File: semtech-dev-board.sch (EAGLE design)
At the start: 62 parts, among them Q1 BSS123, Q2 32MHz, U1 SEMTECH_SX1236, U2 QUALCOMM-TDK_B3588, U3 MIC5219 3.3V, U4 QUALCOMM-TDK_B3710

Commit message: Tuesday D/R
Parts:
- removed C23: 1uF, rcl:C-USC0805
- removed C24, C26, C28: 100nF, rcl:C-USC0805
- removed C27: 10uF, rcl:C-USC0805
- removed CF1: (no value), psas_c3_team05:CON_USB-MICRO-B-RECEPTACLE-PTH-HIROSE-ZX62D-B-5P8
- removed Q2: 32MHz, low-gain-radio:CRYSTAL2.5X2.0MM
- removed S2: SWITCH-MOMENTARY-2SMD-2, psas_c3_team05:SWITCH-MOMENTARY-2SMD-2
- removed TP7: TEST-POINT, low-gain-radio:TEST-POINT
- removed U$1, U$2, U$3, U$4: SMAJ716-ND, psas_c3_team05:SMAJ716-ND
- added C1: 10uF, rcl:C-USC0805
- added C3: 1uF, rcl:C-USC0805
- added P1, P2, P3, P4: SMAJ716-ND, psas_c3_team05:SMAJ716-ND
- added P5: (no value), psas_c3_team05:CON_USB-MICRO-B-RECEPTACLE-PTH-HIROSE-ZX62D-B-5P8
- added S1: SWITCH-MOMENTARY-2SMD-2, psas_c3_team05:SWITCH-MOMENTARY-2SMD-2
- added TP3: TEST-POINT, low-gain-radio:TEST-POINT
- added Y1: 32MHz, low-gain-radio:CRYSTAL2.5X2.0MM
- C11: value 22pF -> 100nF
- C12: value 4.7pF -> 100nF
- C13: value 8.2pF -> 100nF
- C14: value 2.7pF -> 8.2pF
- C15: value ?? -> 10nF
- C16: value 15pF -> 6.8pF
- C17: value ?? -> 5.6pF
- C18: value 6.8pF -> 100nF
- C19: value ?? -> 100nF
- C20: value 8.2pF -> 4.7pF
- C21: value 470pF -> 15pF
- C22: value 5.6pF -> 15pF
- C4: value 100nF -> 470pF
- C5: value 100nF -> 2.7pF
- C6: value 6pF -> 22pF
- C7: value 6pF -> 15pF
- C8: value 10nF -> 8.2pF
- JP1: device pinhead:PINHD-1X7 -> pinhead:PINHD-1X2
- JP2: device pinhead:PINHD-1X4 -> pinhead:PINHD-1X2
- JP3, JP5: device pinhead:PINHD-1X2 -> pinhead:PINHD-1X4
- JP4: device pinhead:PINHD-1X4 -> pinhead:PINHD-1X8
- L1: value 33nH -> 12nH; device rcl:L-USL3230M -> rcl:L-USL3225M
- L2: value 33nH -> 10nH; device rcl:L-USL3230M -> rcl:L-USL3225M
- L3: value 10nH -> 33nH; device rcl:L-USL3230M -> rcl:L-USL3225M
- L4: value 3.9nH -> 10nH; device rcl:L-USL3230M -> rcl:L-USL3225P
- L5: value 12nH -> 33nH; device rcl:L-USL1812 -> rcl:L-USL3225P
- L6: device rcl:L-USL3230M -> rcl:L-USL3225M
- L7: value 10nH -> 6.8nH; device rcl:L-USL3230M -> rcl:L-USL3225M
- L8: value 6.8nH -> 3.9nH; device rcl:L-USL3230M -> rcl:L-USL3225M
- R1: value 1k -> 0
- R5: value 0 -> 1k
- U1: value SEMTECH_SX1236 -> MIC5219 3.3V; device low-gain-radio:SEMTECH_SX1236 -> SparkFun-IC-Power:V_REG_MIC52193.3V
- U2: value QUALCOMM-TDK_B3588 -> QUALCOMM-TDK_B3710; device low-gain-radio:QUALCOMM-TDK_B3588 -> low-gain-radio:QUALCOMM-TDK_B3710
- U3: value MIC5219 3.3V -> QUALCOMM-TDK_B3588; device SparkFun-IC-Power:V_REG_MIC52193.3V -> low-gain-radio:QUALCOMM-TDK_B3588
- U4: value QUALCOMM-TDK_B3710 -> SEMTECH_SX1236; device low-gain-radio:QUALCOMM-TDK_B3710 -> low-gain-radio:SEMTECH_SX1236
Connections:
- removed net DIO0: JP1.2, U1.DIO0
- removed net DIO1: JP1.3, U1.DIO1/DCLK
- removed net DIO2: JP1.4, U1.DIO2/DATA
- removed net DIO3: JP1.5, U1.DIO3
- removed net DIO4: JP1.6, U1.DIO4
- removed net DIO5: JP1.7, U1.DIO5
- new net N$2: JP4.8, U4.DIO5
- new net N$4: JP4.7, U4.DIO4
- new net N$6: JP4.6, U4.DIO3
- new net N$7: JP4.5, U4.DIO2/DATA
- new net N$8: JP4.4, U4.DIO1/DCLK
- new net N$9: JP4.3, U4.DIO0
- net +3V3: now also C3.1, R4.2, R5.2, TP6.1, U1.OUT; no longer C23.1, R1.2, R3.2, TP5.1, U3.OUT
- net BP: now also C4.1, U1.BP; no longer C21.1, U3.BP
- net GND: now also C1.2, C11.2, C13.2, C15.2, C17.2, C19.2, C3.2, JP1.2, JP2.2, P1.OUTERCONDUCTOR, P2.OUTERCONDUCTOR, P3.OUTERCONDUCTOR, P4.OUTERCONDUCTOR, P5.5, S1.1, U1.GND, U4.GND1, U4.GND2, U4.GND3, U4.GROUND; no longer C23.2, C24.2, C26.2, C27.2, C28.2, C5.2, C6.2, CF1.5, JP3.2, JP5.2, S2.1, U$1.OUTERCONDUCTOR, U$2.OUTERCONDUCTOR, U$3.OUTERCONDUCTOR, U$4.OUTERCONDUCTOR, U1.GND1, U1.GND2, U1.GND3, U1.GROUND, U4.GND
- net HFO_PA_HEAD: now also C15.1, JP3.4, L5.2; no longer C9.1, JP4.4, L2.2
- net LED+: now also R3.1; no longer R2.1
- net LFO_PA_HEAD: now also C9.1, JP3.1, L3.2; no longer C8.1, JP4.1, L1.2
- net N$1: now also R2.1, TP4.1, U1.EN; no longer R5.1, TP1.1, U3.EN
- net N$5: now also P1.CENTERCONDUCTOR, U2.OUT; no longer U$1.CENTERCONDUCTOR, U4.OUT
- net PA_BOOST: now also TP2.1, U4.PA_BOOST; no longer TP7.1, U1.PA_BOOST
- net RFI_HF: now also U3.IN, U4.RFI_HF; no longer U1.RFI_HF, U2.IN
- net RFI_HF_ANT: now also P4.CENTERCONDUCTOR, U3.OUT; no longer U$4.CENTERCONDUCTOR, U2.OUT
- net RFI_LF: now also U2.IN, U4.RFI_LF; no longer U1.RFI_LF, U4.IN
- net RFO_HF: now also L8.2, U4.RFO_HF; no longer L4.2, U1.RFO_HF
- net RFO_HF_1: now also C14.2; no longer C13.2, C15.1
- net RFO_HF_2: now also C16.1, L7.2; no longer C15.2, C18.1, C19.1, L8.2
- net RFO_HF_OUT: now also C17.1, L7.1, P3.CENTERCONDUCTOR; no longer C19.2, C22.1, L8.1, U$3.CENTERCONDUCTOR
- net RFO_HF_PA: now also C14.1, C20.1, L5.1, L8.1; no longer C12.1, C13.1, L2.1, L4.1
- net RFO_LF: now also L4.1, U4.RFO_LF; no longer L3.1, U1.RFO_LF
- net RFO_LF_1: now also C5.1, C6.2, L1.2; no longer C11.2, C14.1, L5.2
- net RFO_LF_2: now also C5.2, C7.1, L1.1, L2.2; no longer C14.2, C16.1, C17.1, L5.1, L7.2
- net RFO_LF_OUT: now also C8.1, L2.1, P2.CENTERCONDUCTOR; no longer C17.2, C20.1, L7.1, U$2.CENTERCONDUCTOR
- net RFO_LF_PA: now also C6.1, L3.1, L4.2; no longer C11.1, L1.1, L3.2
- net RXTX: now also JP2.1, JP4.2, U4.RXTX; no longer JP1.1, JP3.1, U1.RXTX
- net SPI_MISO: now also JP5.2, U4.MISO; no longer JP2.2, U1.MISO
- net SPI_MOSI: now also JP5.3, U4.MOSI; no longer JP2.3, U1.MOSI
- net SPI_NSS: now also JP5.4, U4.NSS; no longer JP2.4, U1.NSS
- net SPI_SCK: now also JP5.1, U4.SCK; no longer JP2.1, U1.SCK
- net SX1236_RST: now also JP4.1, R5.1, S1.2, TP1.1, U4.NRESET; no longer R1.1, S2.2, TP4.1, U1.NRESET
- net VBAT: now also C11.1, C12.1, C13.1, R3.2, R4.1, U4.VBAT_ANA, U4.VBAT_DIG, U4.VBAT_RF; no longer C2.1, C24.1, C26.1, R2.2, R3.1, U1.VBAT_ANA, U1.VBAT_DIG, U1.VBAT_RF
- net VREG_IN: now also C1.1, C2.1, R1.2, R2.2, TP5.1, U1.IN; no longer C27.1, C28.1, R4.2, R5.2, TP6.1, U3.IN
- net VR_ANA: now also C18.1, U4.VR_ANA; no longer C4.1, U1.VR_ANA
- net VR_DIG: now also C19.1, U4.VR_DIG; no longer C5.1, U1.VR_DIG
- net VR_PA: now also JP3.2, JP3.3, U4.VR_PA; no longer JP4.2, JP4.3, U1.VR_PA
- net V_IN: now also JP1.1, P5.1, R1.1, TP3.1; no longer CF1.1, JP5.1, R4.1, TP2.1
- net XTALA: now also C22.1, U4.XTA, Y1.2; no longer C7.1, Q2.2, U1.XTA
- net XTALB: now also C21.1, U4.XTB, Y1.1; no longer C6.1, Q2.1, U1.XTB
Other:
- moved on the sheet: C10, C11, C12, C13, C14, C15, C16, C17, C18, C19, C2, C20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

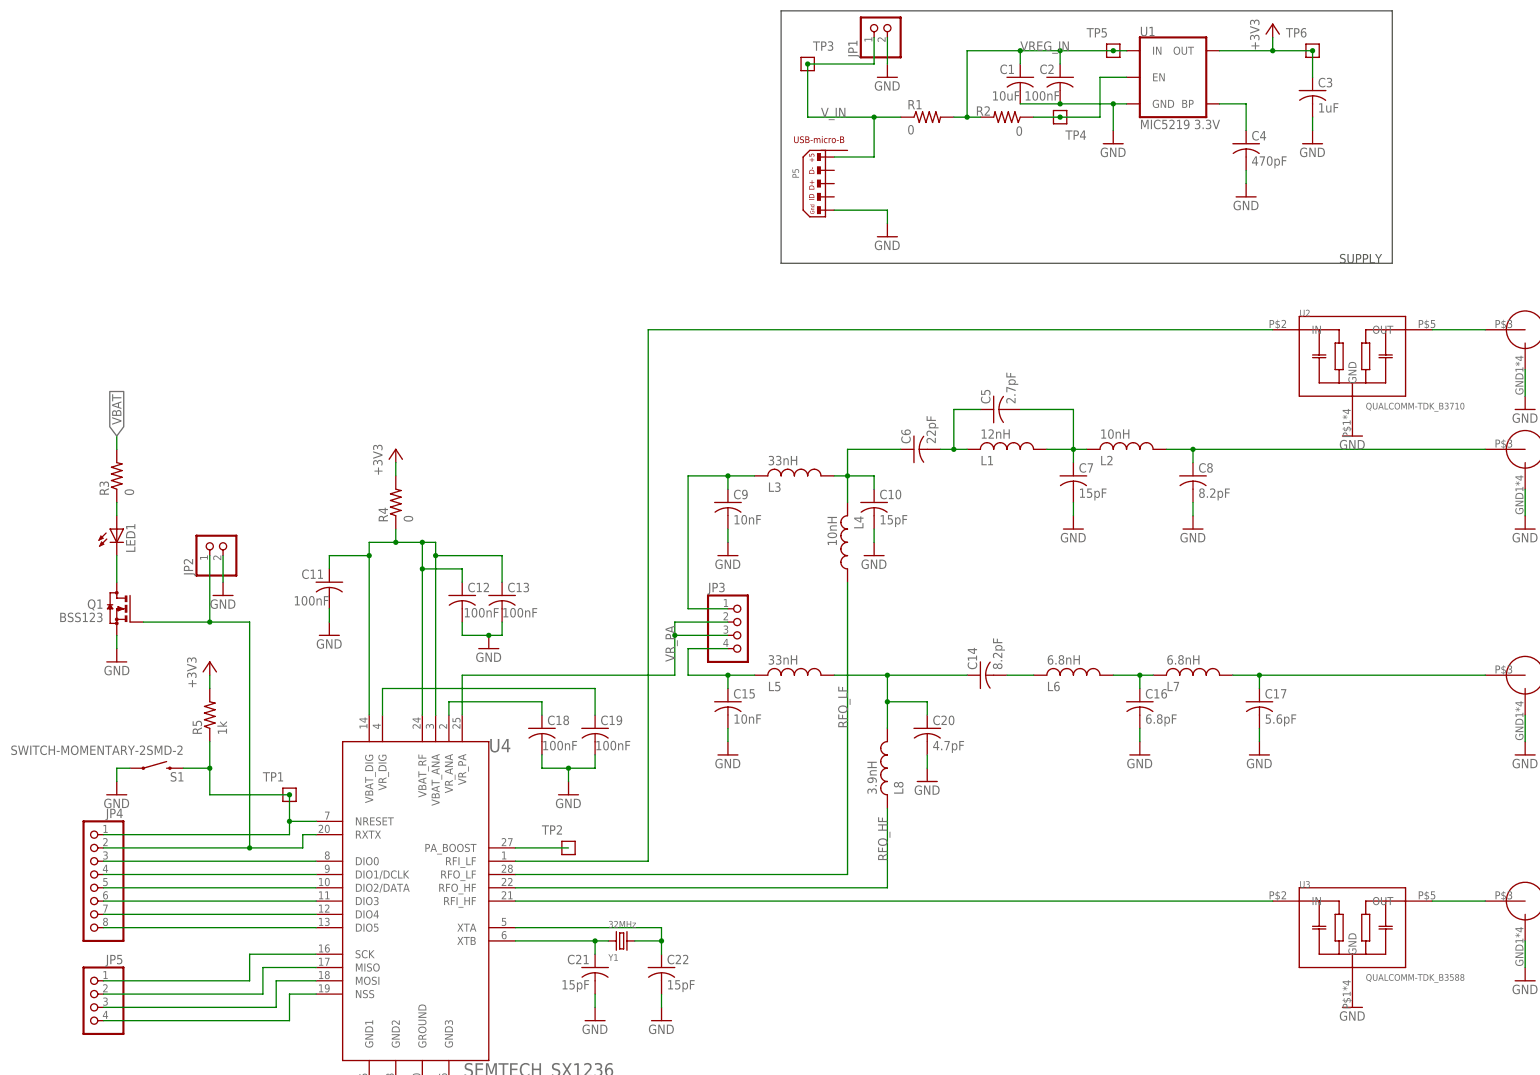
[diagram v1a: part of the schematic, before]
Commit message: reworked board based on feedback, needs mounting holes
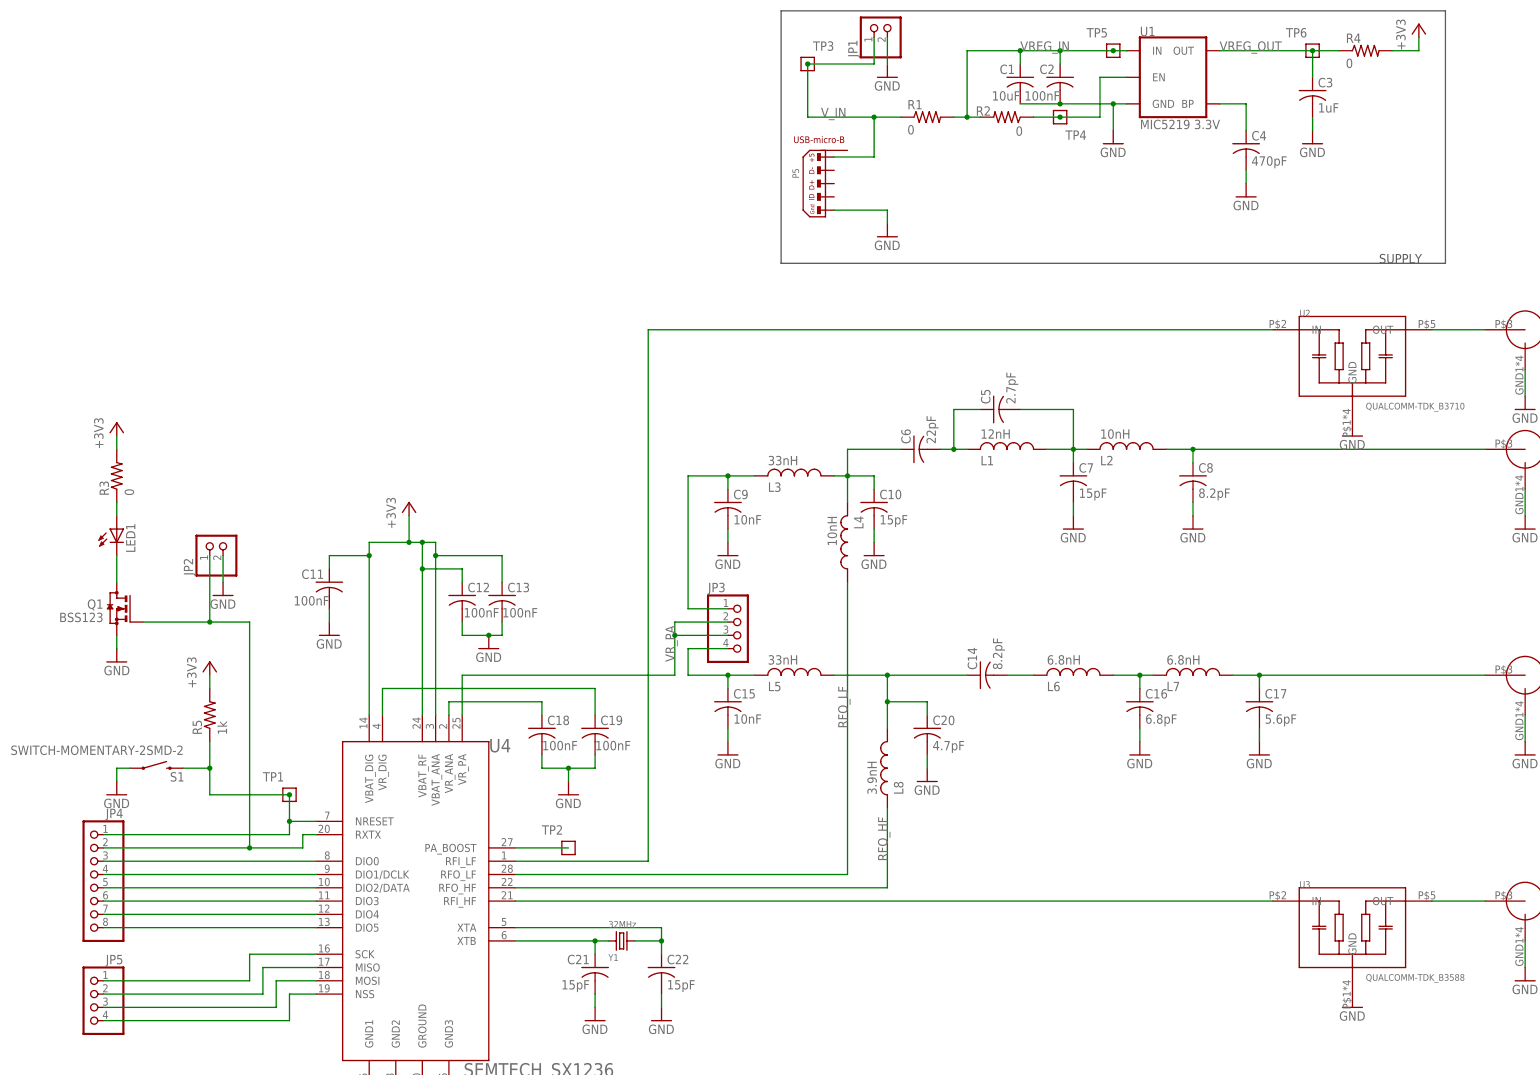
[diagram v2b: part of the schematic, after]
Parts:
- C1, C10, C11, C12, C13, C15, C16, C17, C18, C19, C2, C20, C21, C22, C3, C4, C5, C7, C8, C9: device rcl:C-USC0805 -> rcl_custom:C-USC0603
- R1, R2, R3, R4, R5: device rcl:R-US_R0805 -> rcl_custom:R-US_0603-A
- renumbered P1 to RFO_LF_IN
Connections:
- net N$2 renamed DIO5
- net N$4 renamed DIO4
- net N$5 renamed RFI_LF_ANT
- net N$6 renamed DIO3
- net N$7 renamed DIO2
- net N$8 renamed DIO1
- net N$9 renamed DIO0
- removed net VBAT: C11.1, C12.1, C13.1, R3.2, R4.1, U4.VBAT_ANA, U4.VBAT_DIG, U4.VBAT_RF
- new net VREG_OUT: C3.1, R4.1, TP6.1, U1.OUT
- net +3V3: now also C11.1, C12.1, C13.1, R3.2, U4.VBAT_ANA, U4.VBAT_DIG, U4.VBAT_RF; no longer C3.1, TP6.1, U1.OUT

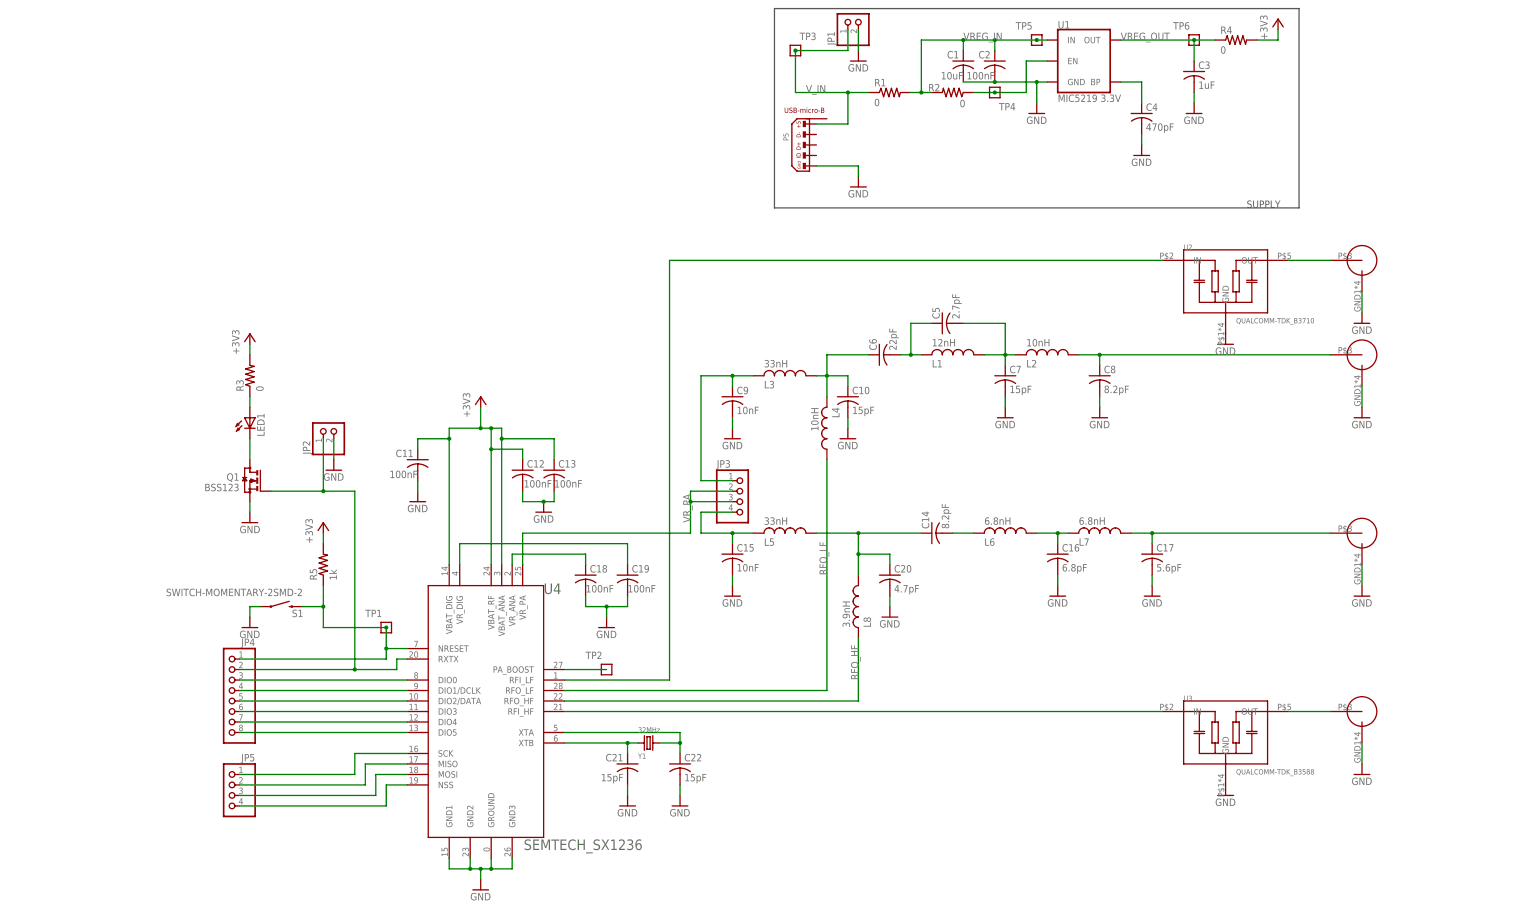
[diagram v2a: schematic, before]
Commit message: Board clean up from Evan's excellent first draft. Fixed SMA connectors, SAW filters, and 1236 packages. Made sure passives were from rlc_custom. More stiching, isolate on polygons, added a mounting hole, made it more symmetric, and rounded off board to mm. Needs one more review, but needs a check in before then.
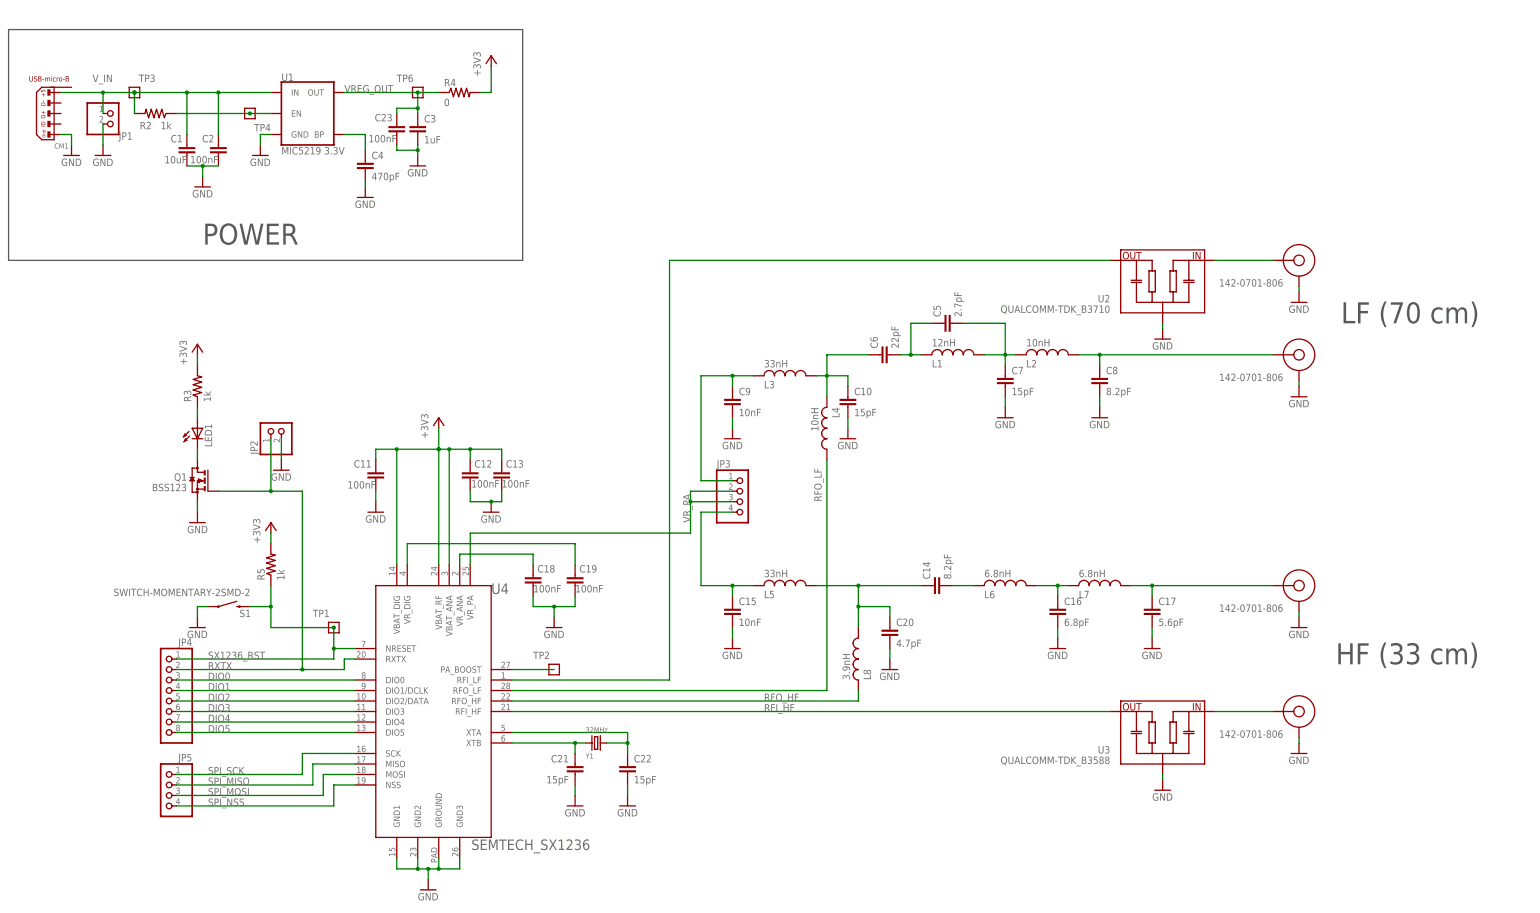
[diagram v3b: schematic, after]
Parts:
- removed P2, P3, P4, RFO_LF_IN: SMAJ716-ND, psas_c3_team05:SMAJ716-ND
- removed P5: (no value), psas_c3_team05:CON_USB-MICRO-B-RECEPTACLE-PTH-HIROSE-ZX62D-B-5P8
- removed R1: 0, rcl_custom:R-US_0603-A
- removed TP5: TEST-POINT, low-gain-radio:TEST-POINT
- added C23: 100nF, rcl_custom:C-EU0603-B-NOSILK
- added CF1, CF2, CF3, CF4: 142-0701-806, psas_c3_team05:SMA-CINCH-END-FIRE
- added CM1: (no value), psas_c3_team05:CON_USB-MICRO-B-RECEPTACLE-PTH-HIROSE-ZX62D-B-5P8
- C1: device rcl_custom:C-USC0603 -> rcl_custom:C-EU0805-B
- C10, C11, C12, C13, C15, C16, C17, C18, C19, C2, C20, C21, C22, C3, C4, C5, C7, C8, C9: device rcl_custom:C-USC0603 -> rcl_custom:C-EU0603-B-NOSILK
- C14, C6: device rcl:C-USC0805 -> rcl_custom:C-EU0603-B-NOSILK
- R2, R3: value 0 -> 1k; device rcl_custom:R-US_0603-A -> rcl_custom:R-US_0603-B-NOSILK
- R4, R5: device rcl_custom:R-US_0603-A -> rcl_custom:R-US_0603-B-NOSILK
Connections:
- removed net RFI_HF_ANT: P4.CENTERCONDUCTOR, U3.OUT
- removed net RFI_LF_ANT: RFO_LF_IN.CENTERCONDUCTOR, U2.OUT
- removed net VREG_IN: C1.1, C2.1, R1.2, R2.2, TP5.1, U1.IN
- new net N$2: CF4.CENTERCONDUCTOR, U3.IN
- new net N$4: CF1.CENTERCONDUCTOR, U2.IN
- net GND: now also C23.2, CF1.GND, CF2.GND, CF3.GND, CF4.GND, CM1.5; no longer P2.OUTERCONDUCTOR, P3.OUTERCONDUCTOR, P4.OUTERCONDUCTOR, P5.5, RFO_LF_IN.OUTERCONDUCTOR
- net RFI_HF: now also U3.OUT; no longer U3.IN
- net RFI_LF: now also U2.OUT; no longer U2.IN
- net RFO_HF_OUT: now also CF3.CENTERCONDUCTOR; no longer P3.CENTERCONDUCTOR
- net RFO_LF_OUT: now also CF2.CENTERCONDUCTOR; no longer P2.CENTERCONDUCTOR
- net VREG_OUT: now also C23.1
- net V_IN: now also C1.1, C2.1, CM1.1, R2.2, U1.IN; no longer P5.1, R1.1
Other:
- note added: "HF (33 cm)"
- note added: "LF (70 cm)"
- note added: "POWER"
- note removed: "SUPPLY"
- moved on the sheet: JP1, JP2, JP4, JP5, L5, L6, L7, L8, LED1, Q1, R2, R3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
